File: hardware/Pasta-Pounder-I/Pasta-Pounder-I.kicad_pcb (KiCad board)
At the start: 2 copper layers, 70 x 27 mm, 61 parts, among them CN1 XT30UPB-M, J1 USB_C_Receptacle, J10 Motor_2-, J11 ESC_VCC, J12 ESC_GND, J4 ESC_Port, J5 JST-SH, J7 Motor_1+, J8 Motor_1-, J9 Motor_2+, Q1 AO3401A, SW1 RESET-SW, SW2 BOOT-SW, SW3 5.8 ZSPT, U1 DRV8874PWPR, U2 DRV8874PWPR, U4 USBLC6-2P6, U5 ESP32S3W1, U7 SY8113BADC

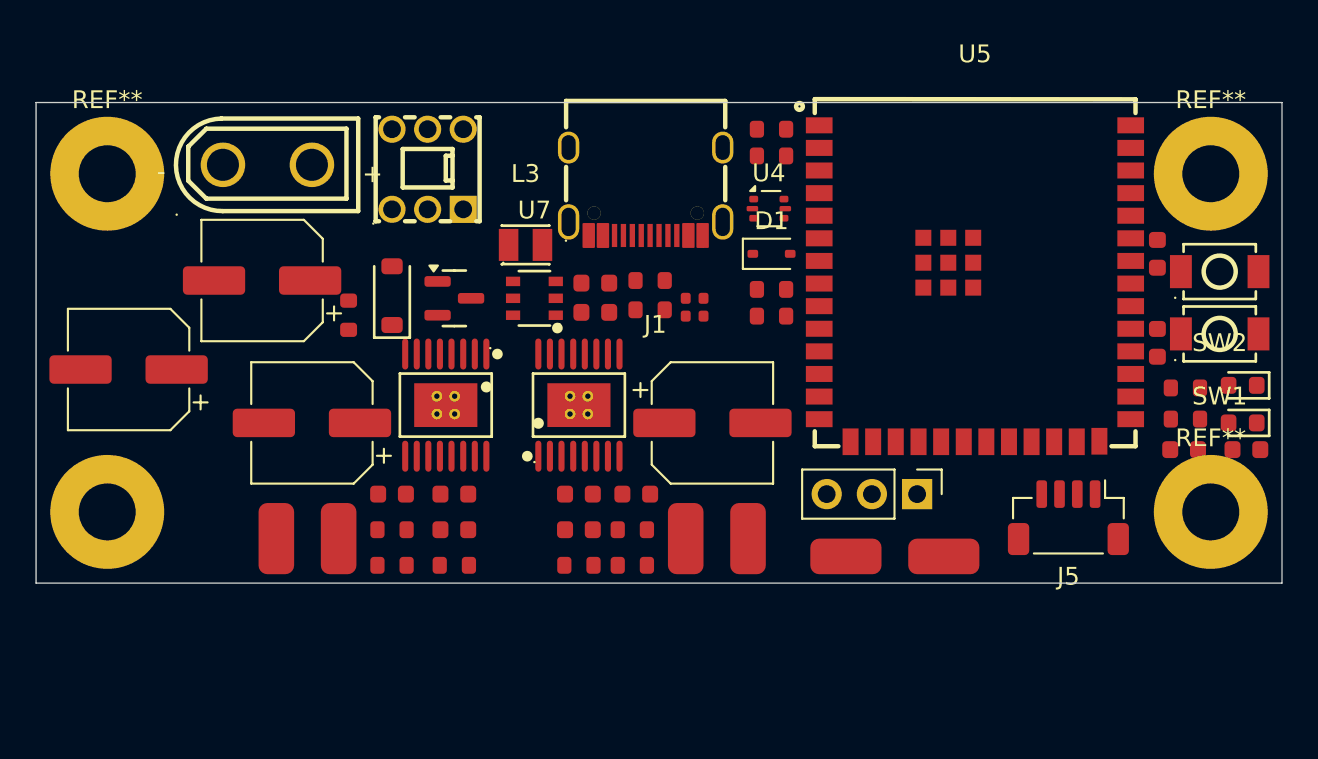
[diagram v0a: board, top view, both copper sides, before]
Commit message: Swapped from WROOM-1U to MINI-1U
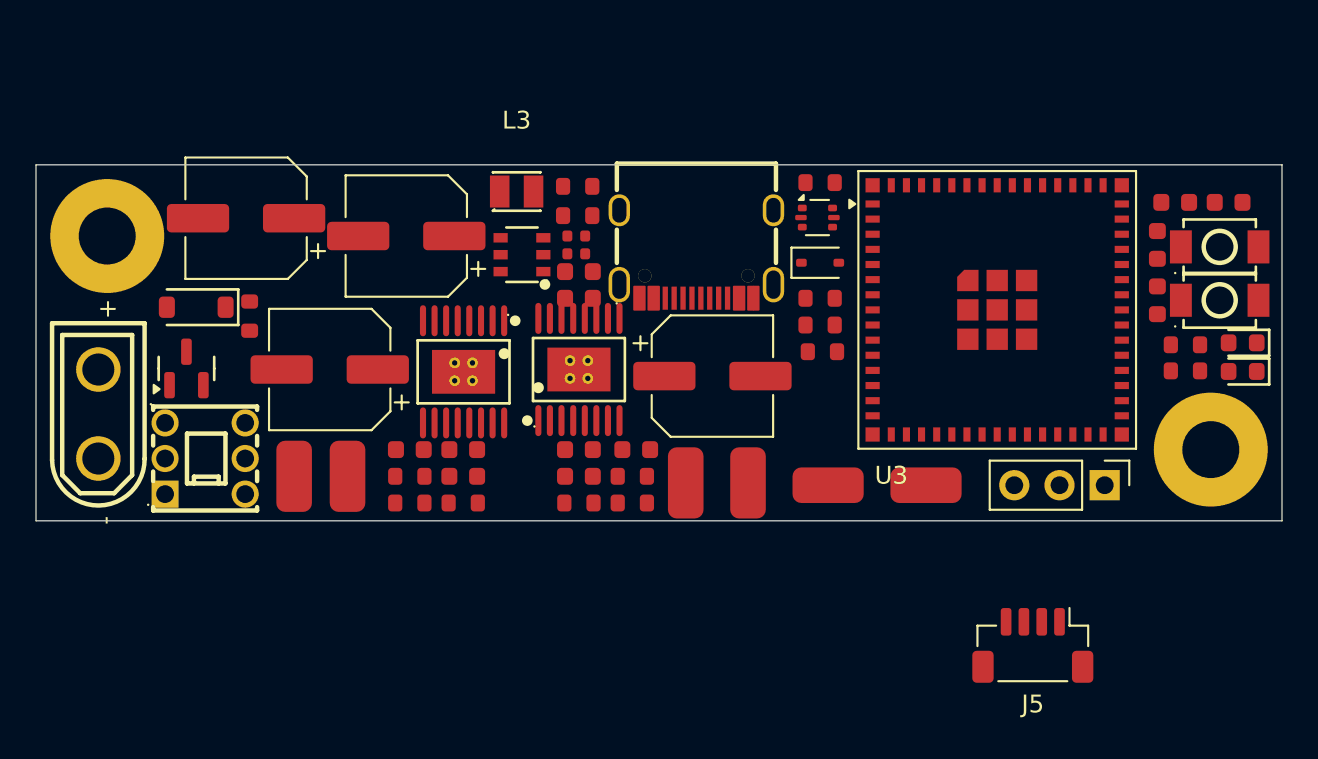
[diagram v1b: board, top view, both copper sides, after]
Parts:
- removed the REF** at (180.5, 90.0)
- removed the REF** at (118.5, 109.0)
- removed U5: ESP32S3W1, lcsc_footprints:C3013946_WIRELM-SMD_ESP32-S3-WROOM-1U
- added U3: ESP32-S3-MINI-1U, RF_Module:ESP32-S2-MINI-1U, F.Cu at (168.5, 97.7)
- moved SW3 20.5 mm to (124.0, 106.0), turned to 90 degrees
- moved CN1 16.9 mm to (118.0, 103.5), turned to 90 degrees
- moved Q1 15.6 mm to (123.0, 100.9), turned to 90 degrees
- moved C2 13.9 mm to (181.5, 91.6)
- moved C1 13.9 mm to (178.5, 91.6)
- moved R1 12.8 mm to (158.7, 100.0), turned to 180 degrees
- moved D2 11.0 mm to (123.5, 97.5), turned to 180 degrees
- moved C14 10.8 mm to (126.3, 92.5)
- moved J4 10.6 mm to (174.5, 107.5)
- moved C13 8.48 mm to (135.3, 93.5)
- moved C27 7.51 mm to (144.8, 93.5)
- moved C28 7.51 mm to (144.8, 94.5)
- moved J5 7.45 mm to (170.5, 116.5)
- moved R12 6.67 mm to (144.9, 90.7)
- moved R13 6.67 mm to (144.9, 92.4)
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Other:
- board size 70 x 27 mm -> 70 x 20 mm

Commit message: Moved components to fully fit within 70x20mm
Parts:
- C12, C8: footprint Capacitor_SMD:CP_Elec_6.3x7.7 -> PCM_JLCPCB:C_0805
- moved J5 19.4 mm to (155.0, 104.8), turned to 90 degrees
- moved J10 10.0 mm to (144.5, 107.0)
- moved J9 9.51 mm to (141.5, 107.0)
- moved R11 7.10 mm to (123.0, 91.8)
- moved U1 7.07 mm to (131.5, 102.0), turned to -90 degrees
- moved C8 5.59 mm to (136.5, 102.0), turned to -90 degrees
- moved C12 3.56 mm to (149.0, 102.0), turned to 90 degrees
- moved C14 2.84 mm to (128.5, 94.3), turned to -90 degrees
- moved C10 2.68 mm to (147.7, 105.5)
- moved C11 2.68 mm to (150.9, 105.5)
- moved C9 2.68 mm to (147.7, 107.0)
- moved R10 2.68 mm to (150.7, 107.0)
- moved R8 2.68 mm to (147.7, 108.5)
- moved R9 2.68 mm to (150.7, 108.5)
- moved U2 1.80 mm to (143.5, 102.0), turned to 90 degrees
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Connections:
- U3 pad 1: Net-(U3-GND-Pad1) -> GND
- U3 pad 2: Net-(U3-GND-Pad1) -> GND
- U3 pad 42: Net-(U3-GND-Pad1) -> GND
- U3 pad 43: Net-(U3-GND-Pad1) -> GND
- U3 pad 46: Net-(U3-GND-Pad1) -> GND
- U3 pad 47: Net-(U3-GND-Pad1) -> GND
- U3 pad 48: Net-(U3-GND-Pad1) -> GND
- U3 pad 49: Net-(U3-GND-Pad1) -> GND
- U3 pad 50: Net-(U3-GND-Pad1) -> GND
- U3 pad 51: Net-(U3-GND-Pad1) -> GND
- U3 pad 52: Net-(U3-GND-Pad1) -> GND
- U3 pad 53: Net-(U3-GND-Pad1) -> GND
- U3 pad 54: Net-(U3-GND-Pad1) -> GND
- U3 pad 55: Net-(U3-GND-Pad1) -> GND
- U3 pad 56: Net-(U3-GND-Pad1) -> GND
- U3 pad 57: Net-(U3-GND-Pad1) -> GND
- U3 pad 58: Net-(U3-GND-Pad1) -> GND
- U3 pad 59: Net-(U3-GND-Pad1) -> GND
- U3 pad 60: Net-(U3-GND-Pad1) -> GND
- U3 pad 61: Net-(U3-GND-Pad1) -> GND
- U3 pad 62: Net-(U3-GND-Pad1) -> GND
- U3 pad 63: Net-(U3-GND-Pad1) -> GND
- U3 pad 64: Net-(U3-GND-Pad1) -> GND
- U3 pad 65: Net-(U3-GND-Pad1) -> GND
